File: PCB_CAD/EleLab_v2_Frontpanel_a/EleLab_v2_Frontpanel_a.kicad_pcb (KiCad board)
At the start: 2 copper layers, 88 x 25 mm, 28 parts, among them J1 Conn_01x04, J10 Conn_01x01, J11 Conn_01x01, J12 Conn_01x01, J13 VBUS, J14 D+, J15 D-, J16 GND, J17 VBUS, J18 D+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

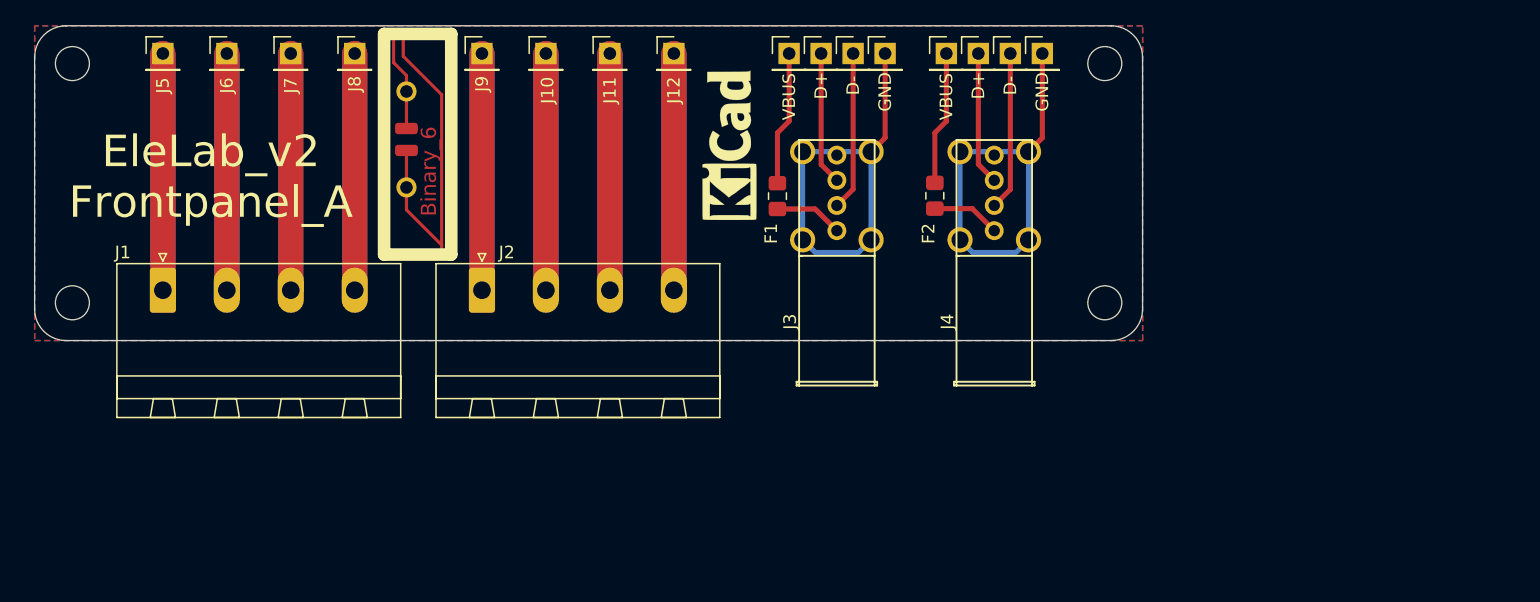
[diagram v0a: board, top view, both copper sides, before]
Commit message: Add files via upload
Made STEP of all files, added more fans and vents to variable PSU, Added iOS charging support to the front panel board, created STLs for the variable power supply. Added model for USB ports.
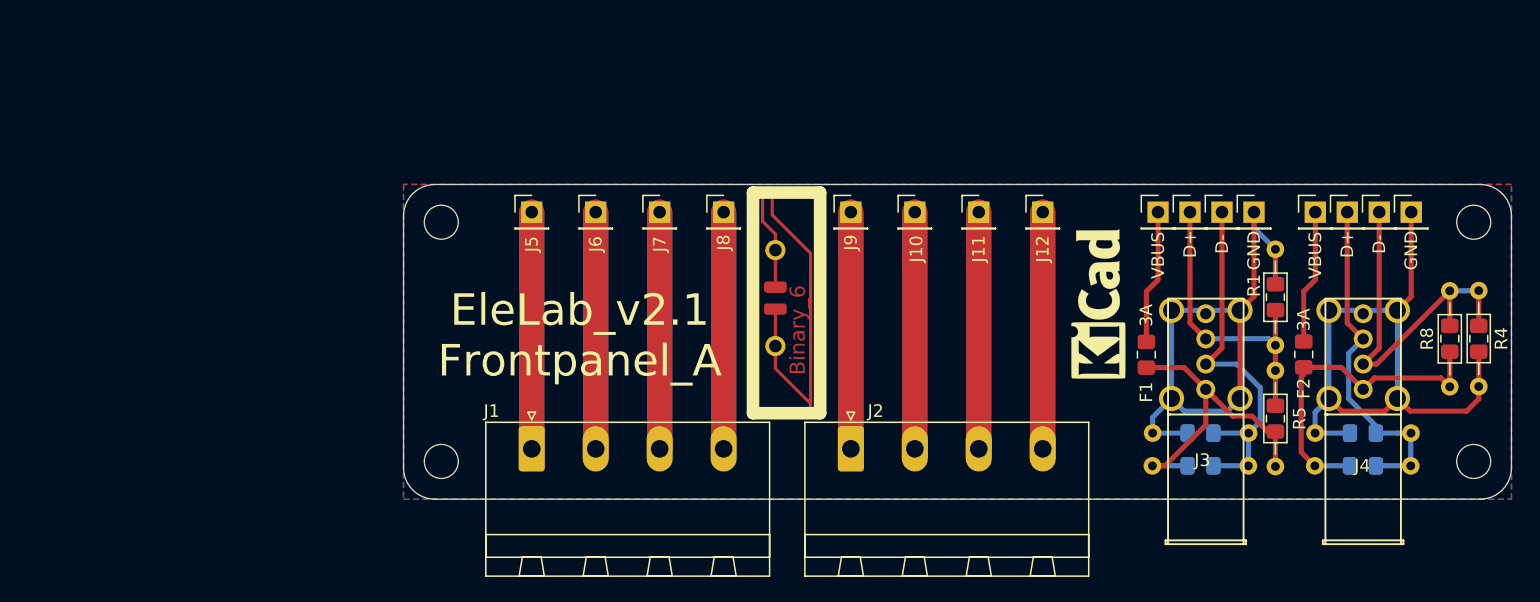
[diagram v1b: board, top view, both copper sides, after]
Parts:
- added R1: 50k, Resistor_THT:R_Axial_DIN0204_L3.6mm_D1.6mm_P7.62mm_Horizontal, F.Cu at (169.6, 91.8)
- added R2: 50k, Resistor_THT:R_Axial_DIN0204_L3.6mm_D1.6mm_P7.62mm_Horizontal, B.Cu at (159.8, 106.3)
- added R3: 50k, Resistor_THT:R_Axial_DIN0204_L3.6mm_D1.6mm_P7.62mm_Horizontal, B.Cu at (172.7, 106.3)
- added R4: 50k, Resistor_THT:R_Axial_DIN0204_L3.6mm_D1.6mm_P7.62mm_Horizontal, F.Cu at (185.7, 102.7)
- added R5: 75k, Resistor_THT:R_Axial_DIN0204_L3.6mm_D1.6mm_P7.62mm_Horizontal, F.Cu at (169.6, 101.4)
- added R6: 75k, Resistor_THT:R_Axial_DIN0204_L3.6mm_D1.6mm_P7.62mm_Horizontal, B.Cu at (167.4, 109.0)
- added R7: 75k, Resistor_THT:R_Axial_DIN0204_L3.6mm_D1.6mm_P7.62mm_Horizontal, B.Cu at (180.3, 109.0)
- added R8: 75k, Resistor_THT:R_Axial_DIN0204_L3.6mm_D1.6mm_P7.62mm_Horizontal, F.Cu at (183.4, 95.0)
- added REF**: R_0805_2012Metric_Pad1.15x1.40mm_HandSolder, Resistor_SMD:R_0805_2012Metric_Pad1.15x1.40mm_HandSolder, F.Cu at (169.6, 95.5)
- added REF**: R_0805_2012Metric_Pad1.15x1.40mm_HandSolder, Resistor_SMD:R_0805_2012Metric_Pad1.15x1.40mm_HandSolder, F.Cu at (169.6, 105.2)
- added REF**: R_0805_2012Metric_Pad1.15x1.40mm_HandSolder, Resistor_SMD:R_0805_2012Metric_Pad1.15x1.40mm_HandSolder, B.Cu at (163.6, 106.3)
- added REF**: R_0805_2012Metric_Pad1.15x1.40mm_HandSolder, Resistor_SMD:R_0805_2012Metric_Pad1.15x1.40mm_HandSolder, B.Cu at (163.6, 109.0)
- added REF**: R_0805_2012Metric_Pad1.15x1.40mm_HandSolder, Resistor_SMD:R_0805_2012Metric_Pad1.15x1.40mm_HandSolder, B.Cu at (176.5, 106.3)
- added REF**: R_0805_2012Metric_Pad1.15x1.40mm_HandSolder, Resistor_SMD:R_0805_2012Metric_Pad1.15x1.40mm_HandSolder, B.Cu at (176.5, 109.0)
- added REF**: R_0805_2012Metric_Pad1.15x1.40mm_HandSolder, Resistor_SMD:R_0805_2012Metric_Pad1.15x1.40mm_HandSolder, F.Cu at (183.4, 98.8)
- added REF**: R_0805_2012Metric_Pad1.15x1.40mm_HandSolder, Resistor_SMD:R_0805_2012Metric_Pad1.15x1.40mm_HandSolder, F.Cu at (185.7, 98.8)
- moved J3 31.9 mm to (161.0, 95.7)
- moved J4 31.9 mm to (173.5, 95.7)
- moved F1 31.9 mm to (159.3, 100.1)
- moved F2 31.9 mm to (171.8, 100.1)
- moved H2 31.9 mm to (185.3, 89.6)
- moved H4 31.9 mm to (185.3, 108.6)
- moved J11 31.9 mm to (146.0, 88.8)
- moved J14 31.9 mm to (162.8, 88.8)
- moved J15 31.9 mm to (165.3, 88.8)
- moved J17 31.9 mm to (172.7, 88.8)
- moved J18 31.9 mm to (175.3, 88.8)
- moved J2 31.9 mm to (135.8, 107.6)
- moved J20 31.9 mm to (180.3, 88.8)
- moved J9 31.9 mm to (135.8, 88.8)
- moved LO_1 31.9 mm to (130.8, 95.6)
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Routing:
- net Net-(F2-Pad1): track 5.44 -> 26.9 mm
- net Net-(F1-Pad1): track 5.43 -> 26.3 mm
- net Net-(J15-Pad1): track 12.6 -> 29.9 mm
- net Net-(J19-Pad1): track 12.6 -> 29.8 mm
- net Net-(J18-Pad1): track 10.6 -> 27.6 mm
- net Net-(J20-Pad1): track 34.2 -> 51.2 mm
- net Net-(J14-Pad1): track 10.6 -> 23.9 mm
- net Net-(J16-Pad1): track 34.2 -> 46.8 mm
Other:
- board text added: "EleLab_v2.1 Frontpanel_A"
- board text removed: "EleLab_v2 Frontpanel_A"
